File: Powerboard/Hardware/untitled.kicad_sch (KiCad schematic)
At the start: 7 parts, among them J3 USB_C_Receptacle_USB2.0

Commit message: waiting for review
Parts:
- removed TP3: TestPoint, TestPoint:TestPoint_Pad_D1.0mm, symbol Connector:TestPoint
- J3: footprint Connector_USB:USB_C_Receptacle_GCT_USB4085 -> Connector_USB:USB_C_Receptacle_Palconn_UTC16-G
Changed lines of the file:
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@@
-    (stroke (width 0) (type default) (color 0 0 0 0))
-  )
-  (wire (pts (xy 68.834 95.758) (xy 76.454 95.758))
     (stroke (width 0) (type default) (color 0 0 0 0))
   )
@@
     (effects (font (size 1.27 1.27)) (justify left bottom))
   )
-  (label "VBUS" (at 68.834 95.758 0)
-    (effects (font (size 1.27 1.27)) (justify left bottom))
-  )
   (label "VBUS" (at 153.924 121.158 90)
     (effects (font (size 1.27 1.27)) (justify left bottom))
@@
     )
     (property "Datasheet" "~" (id 3) (at 76.454 95.758 0)
-      (effects (font (size 1.27 1.27)) hide)
-    )
-    (pin "1")
-  )
-  (symbol (lib_id "Connector:TestPoint") (at 76.454 95.758 270) (unit 1)
-    (in_bom yes) (on_board yes)
-    (property "Reference" "TP3" (id 0) (at 81.2292 94.5896 90)
-      (effects (font (size 1.27 1.27)) (justify left))
-    )
-    (property "Value" "TestPoint" (id 1) (at 81.2292 96.901 90)
-      (effects (font (size 1.27 1.27)) (justify left))
-    )
-    (property "Footprint" "TestPoint:TestPoint_Pad_D1.0mm" (id 2) (at 76.454 100.838 0)
-      (effects (font (size 1.27 1.27)) hide)
-    )
-    (property "Datasheet" "~" (id 3) (at 76.454 100.838 0)
       (effects (font (size 1.27 1.27)) hide)
     )
@@
     (property "Reference" "J3" (id 0) (at 127.4318 68.6562 0))
     (property "Value" "USB_C_Receptacle_USB2.0" (id 1) (at 127.4318 70.9676 0))
-    (property "Footprint" "Connector_USB:USB_C_Receptacle_GCT_USB4085" (id 2) (at 128.524 90.678 0)
+    (property "Footprint" "Connector_USB:USB_C_Receptacle_Palconn_UTC16-G" (id 2) (at 128.524 90.678 0)
       (effects (font (size 1.27 1.27)) hide)
     )

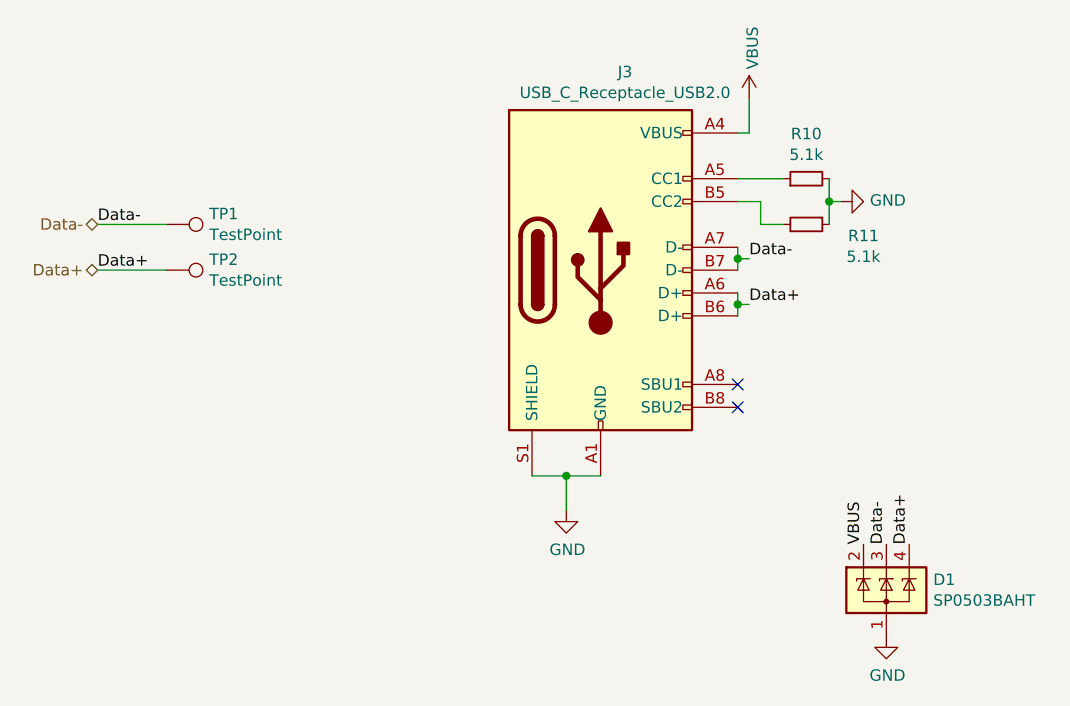
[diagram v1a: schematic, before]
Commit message: i2c breakout, general clean up
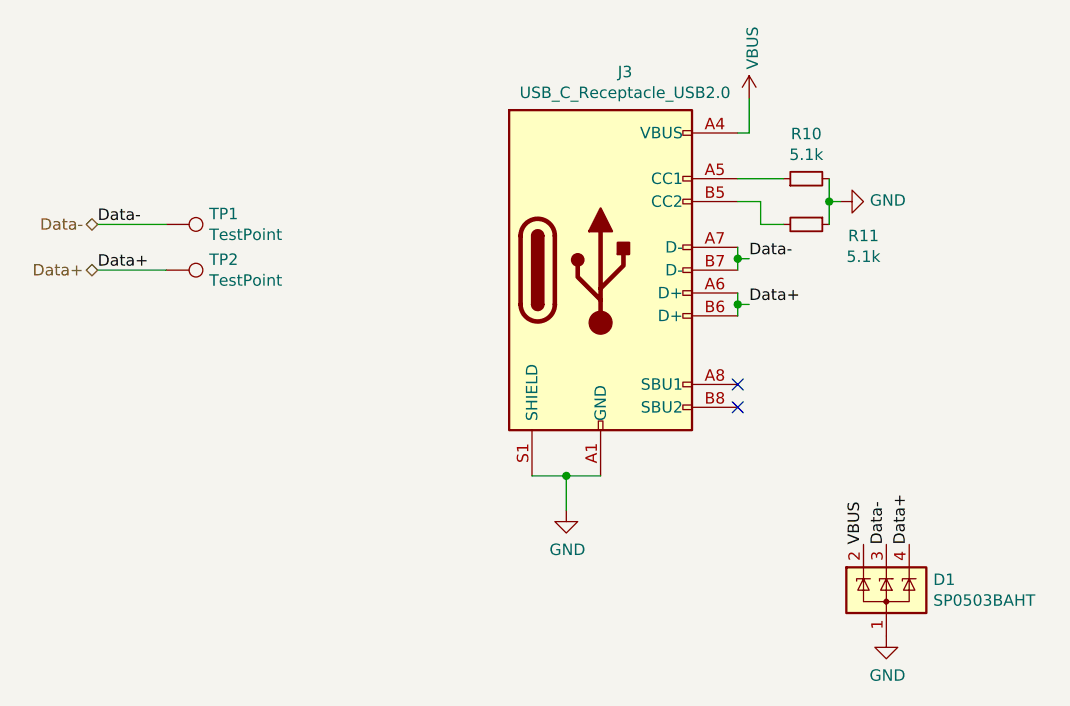
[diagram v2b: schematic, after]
